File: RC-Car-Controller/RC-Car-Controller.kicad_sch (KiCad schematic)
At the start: 4 parts

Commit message: Fixed Controller PCB
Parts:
- D1, D2: footprint (none) -> LED_SMD:LED_0201_0603Metric
- R13: value R -> 1.5kohm; footprint (none) -> Resistor_SMD:R_0201_0603Metric
- R14: footprint (none) -> Resistor_SMD:R_0201_0603Metric
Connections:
- no-connect marks 3 -> 4
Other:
- removed sheet CurrentSense
- added sheet MiscDriver (MiscDriver.kicad_sch)
- sheet Connectors ports: added LIGHTS_PWM, NRST, RELAY_CTRL, RF_ANT, SWCLK, SWDIO, USART_RX, USART_TX; removed none
- sheet MCU ports: added LIGHTS_PWM, NRST, RELAY_CTRL, RF_NRST, SPI1_CS_RF, SPI1_MISO_RF, SPI1_MOSI_RF, SPI1_SCLK_RF, SWCLK, SWDIO, USART1_RX, USART1_TX; removed none
- sheet RF ports: added CS, IRQ, MISO, MOSI, RF_ANT, RSTN, SCLK; removed none
- note added: "Power"
- note removed: "Main"
- note removed: "Power Domains"

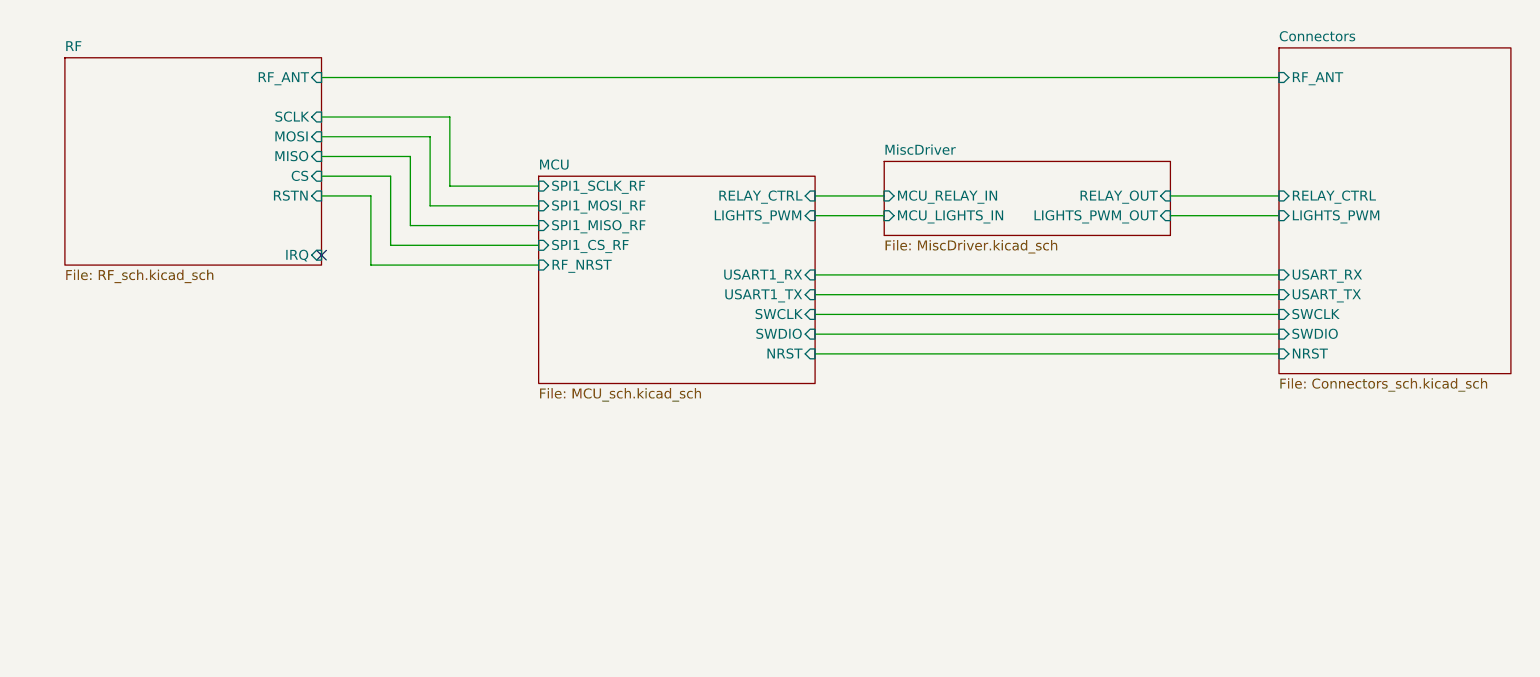
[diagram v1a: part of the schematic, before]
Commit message: Added IO to Controller
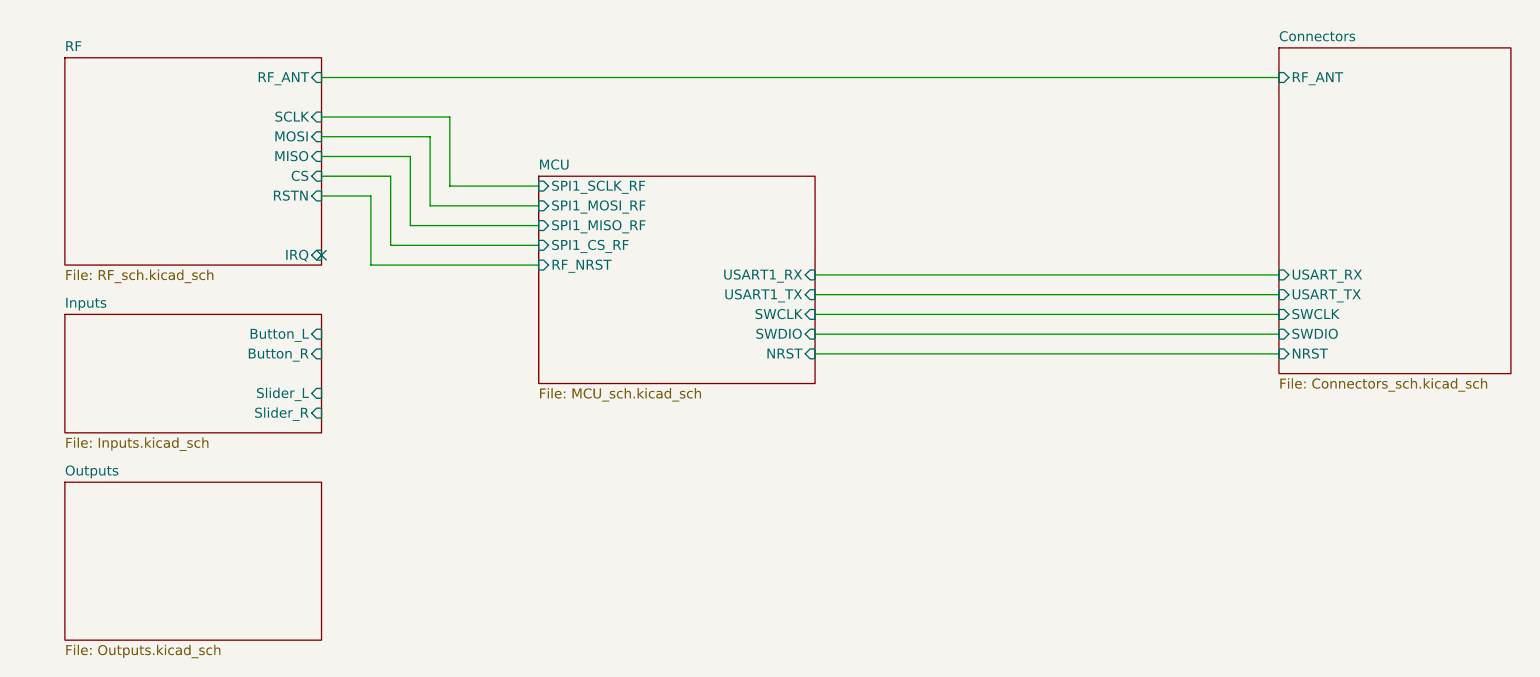
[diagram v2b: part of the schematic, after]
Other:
- removed sheet MiscDriver
- added sheet Inputs (Inputs.kicad_sch)
- added sheet Outputs (Outputs.kicad_sch)
- sheet Connectors ports: added none; removed LIGHTS_PWM, RELAY_CTRL
- sheet MCU ports: added none; removed LIGHTS_PWM, RELAY_CTRL
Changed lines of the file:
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@@
-	(wire
-		(pts
-			(xy 194.31 87.63) (xy 208.28 87.63)
-		)
-		(stroke
-			(width 0)
-			(type default)
-		)
-	)
 	(wire
 		(pts
@@
 	(wire
 		(pts
-			(xy 148.59 87.63) (xy 157.48 87.63)
-		)
-		(stroke
-			(width 0)
-			(type default)
-		)
-	)
-	(wire
-		(pts
 			(xy 85.09 80.01) (xy 96.52 80.01)
 		)
@@
 	(wire
 		(pts
-			(xy 148.59 85.09) (xy 157.48 85.09)
-		)
-		(stroke
-			(width 0)
-			(type default)
-		)
-	)
-	(wire
-		(pts
 			(xy 113.03 86.36) (xy 99.06 86.36)
-		)
-		(stroke
-			(width 0)
-			(type default)
-		)
-	)
-	(wire
-		(pts
-			(xy 194.31 85.09) (xy 208.28 85.09)
 		)
 		(stroke
@@
 	)
 	(sheet
+		(at 52.07 100.33)
+		(size 33.02 15.24)
+		(fields_autoplaced yes)
+		(stroke
+			(width 0.1524)
+			(type solid)
+		)
+		(fill
+			(color 0 0 0 0.0000)
+		)
+		(property "Sheetname" "Inputs"
+			(at 52.07 99.6184 0)
+			(effects
+				(font
+					(size 1.27 1.27)
+				)
+				(justify left bottom)
+			)
+		)
+		(property "Sheetfile" "Inputs.kicad_sch"
+			(at 52.07 116.1546 0)
+			(effects
+				(font
+					(size 1.27 1.27)
+				)
+				(justify left top)
+			)
+		)
+		(pin "Button_L" input
+			(at 85.09 102.87 0)
+			(effects
+				(font
+					(size 1.27 1.27)
+				)
+				(justify right)
+			)
+		)
+		(pin "Slider_R" input
+			(at 85.09 113.03 0)
+			(effects
+				(font
+					(size 1.27 1.27)
+				)
+				(justify right)
+			)
+		)
+		(pin "Slider_L" input
+			(at 85.09 110.49 0)
+			(effects
+				(font
+					(size 1.27 1.27)
+				)
+				(justify right)
+			)
+		)
+		(pin "Button_R" input
+			(at 85.09 105.41 0)
+			(effects
+				(font
+					(size 1.27 1.27)
+				)
+				(justify right)
+			)
+		)
+		(instances
+			(project "RC-Car-Controller"
+				(path "/ba870fd1-751d-4755-8e1a-1ea86ca9e2f6"
+					(page "7")
+				)
+			)
+		)
+	)
+	(sheet
 		(at 208.28 66.04)
 		(size 29.845 41.91)
@@
 				)
 				(justify left top)
-			)
-		)
-		(pin "RELAY_CTRL" input
-			(at 208.28 85.09 180)
-			(effects
-				(font
-					(size 1.27 1.27)
-				)
-				(justify left)
-			)
-		)
-		(pin "LIGHTS_PWM" input
-			(at 208.28 87.63 180)
-			(effects
-				(font
-					(size 1.27 1.27)
-				)
-				(justify left)
 			)
 		)
@@
 	)
 	(sheet
-		(at 157.48 80.645)
-		(size 36.83 9.525)
+		(at 113.03 82.55)
+		(size 35.56 26.67)
 		(fields_autoplaced yes)
 		(stroke
@@
 			(color 0 0 0 0.0000)
 		)
-		(property "Sheetname" "MiscDriver"
-			(at 157.48 79.9334 0)
+		(property "Sheetname" "MCU"
+			(at 113.03 81.8384 0)
 			(effects
 				(font
@@
 			)
 		)
-		(property "Sheetfile" "MiscDriver.kicad_sch"
-			(at 157.48 90.7546 0)
+		(property "Sheetfile" "MCU_sch.kicad_sch"
+			(at 113.03 109.8046 0)
 			(effects
 				(font
@@
 			)
 		)
-		(pin "MCU_RELAY_IN" input
-			(at 157.48 85.09 180)
+		(pin "SPI1_MISO_RF" input
+			(at 113.03 88.9 180)
 			(effects
 				(font
@@
 			)
 		)
-		(pin "MCU_LIGHTS_IN" input
-			(at 157.48 87.63 180)
+		(pin "SPI1_MOSI_RF" input
+			(at 113.03 86.36 180)
 			(effects
 				(font
@@
 			)
 		)
-		(pin "LIGHTS_PWM_OUT" input
-			(at 194.31 87.63 0)
-			(effects
-				(font
-					(size 1.27 1.27)
-				)
-				(justify right)
-			)
-		)
-		(pin "RELAY_OUT" input
-			(at 194.31 85.09 0)
-			(effects
-				(font
-					(size 1.27 1.27)
-				)
-				(justify right)
+		(pin "SPI1_SCLK_RF" input
+			(at 113.03 83.82 180)
+			(effects
+				(font
+					(size 1.27 1.27)
+				)
+				(justify left)
+			)
+		)
+		(pin "USART1_TX" input
+			(at 148.59 97.79 0)
+			(effects
+				(font
+					(size 1.27 1.27)
+				)
+				(justify right)
+			)
+		)
+		(pin "USART1_RX" input
+			(at 148.59 95.25 0)
+			(effects
+				(font
+					(size 1.27 1.27)
+				)
+				(justify right)
+			)
+		)
+		(pin "SPI1_CS_RF" input
+			(at 113.03 91.44 180)
+			(effects
+				(font
+					(size 1.27 1.27)
+				)
+				(justify left)
+			)
+		)
+		(pin "NRST" input
+			(at 148.59 105.41 0)
+			(effects
+				(font
+					(size 1.27 1.27)
+				)
+				(justify right)
+			)
+		)
+		(pin "SWDIO" input
+			(at 148.59 102.87 0)
+			(effects
+				(font
+					(size 1.27 1.27)
+				)
+				(justify right)
+			)
+		)
+		(pin "SWCLK" input
+			(at 148.59 100.33 0)
+			(effects
+				(font
+					(size 1.27 1.27)
+				)
+				(justify right)
+			)
+		)
+		(pin "RF_NRST" input
+			(at 113.03 93.98 180)
+			(effects
+				(font
+					(size 1.27 1.27)
+				)
+				(justify left)
 			)
 		)
@@
 			(project "RC-Car-Controller"
 				(path "/ba870fd1-751d-4755-8e1a-1ea86ca9e2f6"
-					(page "8")
+					(page "4")
 				)
 			)
@@
 	)
 	(sheet
-		(at 113.03 82.55)
-		(size 35.56 26.67)
+		(at 52.07 121.92)
+		(size 33.02 20.32)
 		(fields_autoplaced yes)
 		(stroke
@@
 			(color 0 0 0 0.0000)
 		)
-		(property "Sheetname" "MCU"
-			(at 113.03 81.8384 0)
+		(property "Sheetname" "Outputs"
+			(at 52.07 121.2084 0)
 			(effects
 				(font
@@
 			)
 		)
-		(property "Sheetfile" "MCU_sch.kicad_sch"
-			(at 113.03 109.8046 0)
+		(property "Sheetfile" "Outputs.kicad_sch"
+			(at 52.07 142.8246 0)
 			(effects
 				(font
@@
 			)
 		)
-		(pin "SPI1_MISO_RF" input
-			(at 113.03 88.9 180)
-			(effects
-				(font
-					(size 1.27 1.27)
-				)
-				(justify left)
-			)
-		)
-		(pin "SPI1_MOSI_RF" input
-			(at 113.03 86.36 180)
-			(effects
-				(font
-					(size 1.27 1.27)
-				)
-				(justify left)
-			)
-		)
-		(pin "SPI1_SCLK_RF" input
-			(at 113.03 83.82 180)
-			(effects
-				(font
-					(size 1.27 1.27)
-				)
-				(justify left)
-			)
-		)
-		(pin "USART1_TX" input
-			(at 148.59 97.79 0)
-			(effects
-				(font
-					(size 1.27 1.27)
-				)
-				(justify right)
-			)
-		)
-		(pin "USART1_RX" input
-			(at 148.59 95.25 0)
-			(effects
-				(font
-					(size 1.27 1.27)
-				)
-				(justify right)
-			)
-		)
-		(pin "RELAY_CTRL" input
-			(at 148.59 85.09 0)
-			(effects
-				(font
-					(size 1.27 1.27)
-				)
-				(justify right)
-			)
-		)
-		(pin "SPI1_CS_RF" input
-			(at 113.03 91.44 180)
-			(effects
-				(font
-					(size 1.27 1.27)
-				)
-				(justify left)
-			)
-		)
-		(pin "NRST" input
-			(at 148.59 105.41 0)
-			(effects
-				(font
-					(size 1.27 1.27)
-				)
-				(justify right)
-			)
-		)
-		(pin "SWDIO" input
-			(at 148.59 102.87 0)
-			(effects
-				(font
-					(size 1.27 1.27)
-				)
-				(justify right)
-			)
-		)
-		(pin "SWCLK" input
-			(at 148.59 100.33 0)
-			(effects
-				(font
-					(size 1.27 1.27)
-				)
-				(justify right)
-			)
-		)
-		(pin "RF_NRST" input
-			(at 113.03 93.98 180)
-			(effects
-				(font
-					(size 1.27 1.27)
-				)
-				(justify left)
-			)
-		)
-		(pin "LIGHTS_PWM" input
-			(at 148.59 87.63 0)
-			(effects
-				(font
-					(size 1.27 1.27)
-				)
-				(justify right)
-			)
-		)
 		(instances
 			(project "RC-Car-Controller"
 				(path "/ba870fd1-751d-4755-8e1a-1ea86ca9e2f6"
-					(page "4")
-				)
-			)
+					(page "8")
+				)
+			)

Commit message: Finished prelim. Controller
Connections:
- no-connect marks 4 -> 6
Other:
- added sheet ADC (adc.kicad_sch)
- sheet MCU ports: added ALERT_GPIO, BTN_L, BTN_R, I2C1_SCL, I2C1_SDA, I2C2_SCL, I2C2_SDA, SPI2_CS_LCD, SPI2_MISO, SPI2_MOSI, SPI2_SCLK, SPI3_CS_ADC, SPI3_MISO, SPI3_MOSI, SPI3_SCLK, SPI4_CS_RF, SPI4_MISO_RF, SPI4_MOSI_RF, SPI4_SCLK_RF, WIPE_L, WIPE_R; removed SPI1_CS_RF, SPI1_MISO_RF, SPI1_MOSI_RF, SPI1_SCLK_RF
- sheet Outputs ports: added LCD_CLK, LCD_CS, LCD_DC, LCD_DIN, LCD_RST, OLED_L_SCL, OLED_L_SDA, OLED_R_SCL, OLED_R_SDA; removed none

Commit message: Did some stuff on the Controller
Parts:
- removed R13: 1.5kohm, Resistor_SMD:R_0201_0603Metric, symbol Device:R
- removed R14: 220ohm, Resistor_SMD:R_0201_0603Metric, symbol Device:R
- added R7: 1.5kohm, Resistor_SMD:R_0603_1608Metric, symbol Device:R
- added R8: 220ohm, Resistor_SMD:R_0603_1608Metric, symbol Device:R
- D1, D2: footprint LED_SMD:LED_0201_0603Metric -> LED_SMD:LED_0603_1608Metric
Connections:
- net +3V3: now also R8.1
- net VDD_BATT: now also R7.1
- net at D1.2 (A): now also R7.2
- net at D2.2 (A): now also R8.2
- no-connect marks 6 -> 8
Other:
- sheet Connectors ports: added CON_USB_D+, CON_USB_D-; removed none
- sheet MCU ports: added MCU_USB_D+, MCU_USB_D-; removed none
- note added: "SWITCH"

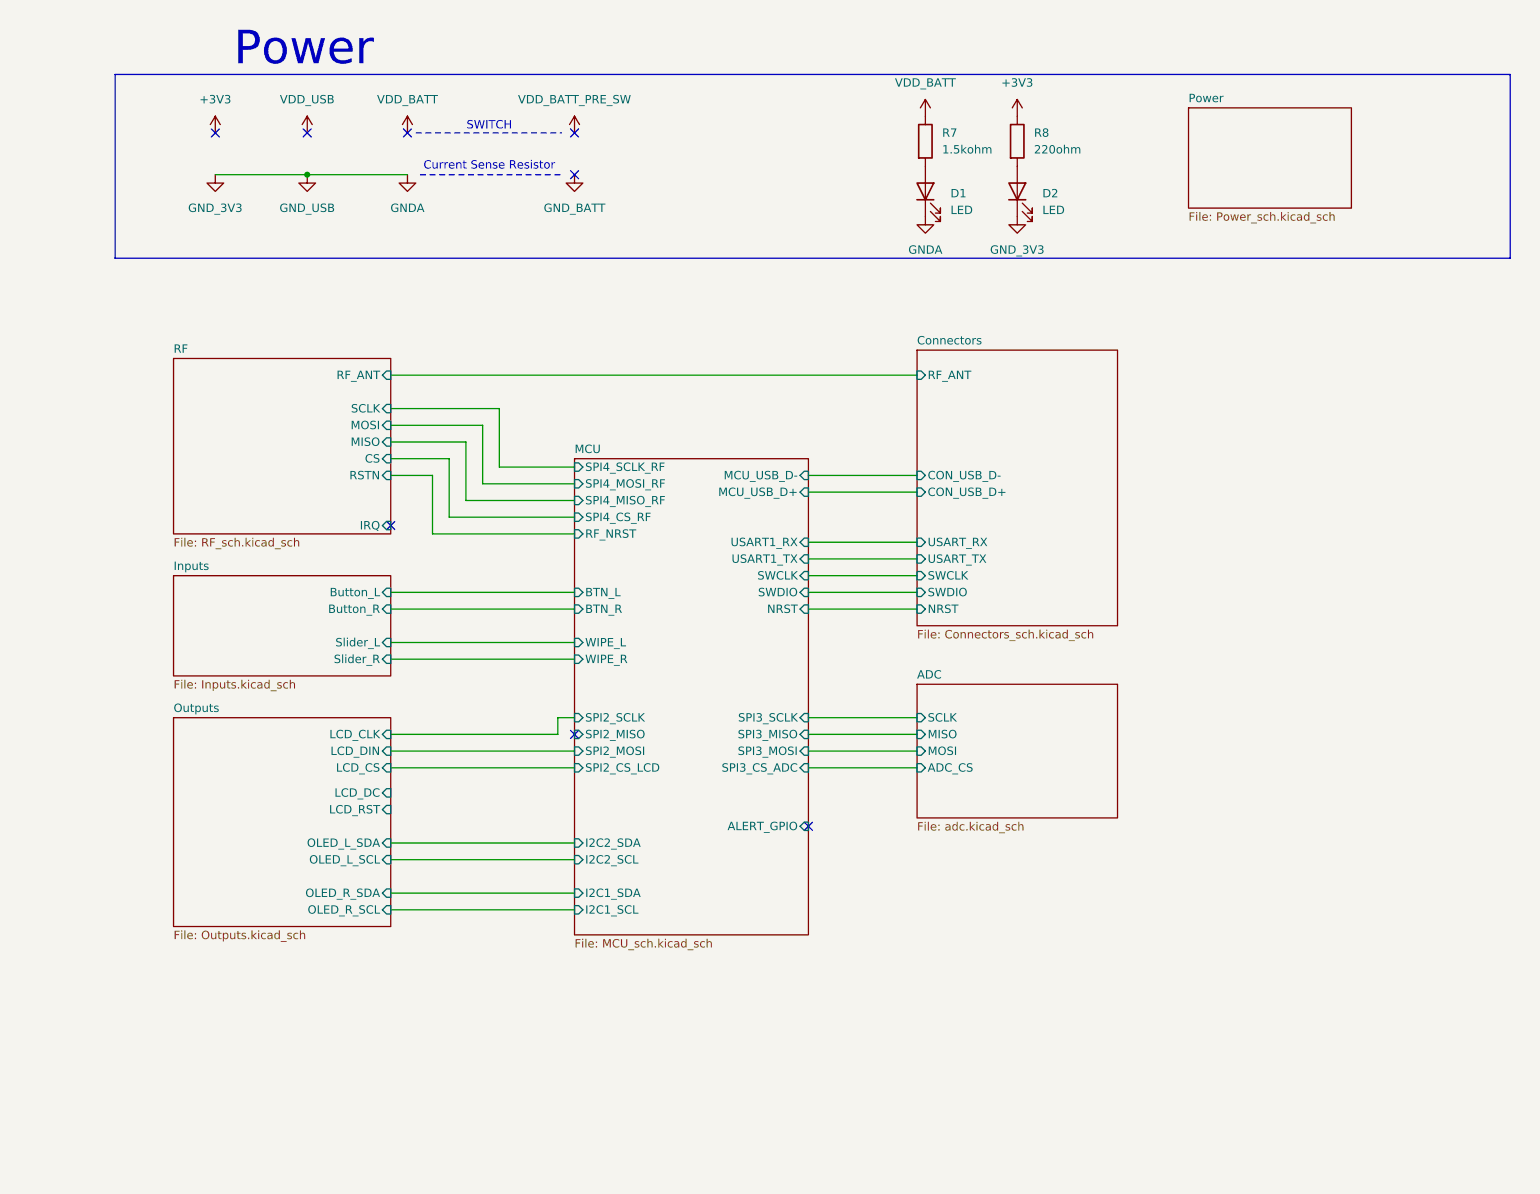
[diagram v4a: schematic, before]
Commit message: Fixed LiPo Charge/Monitor Circuitry
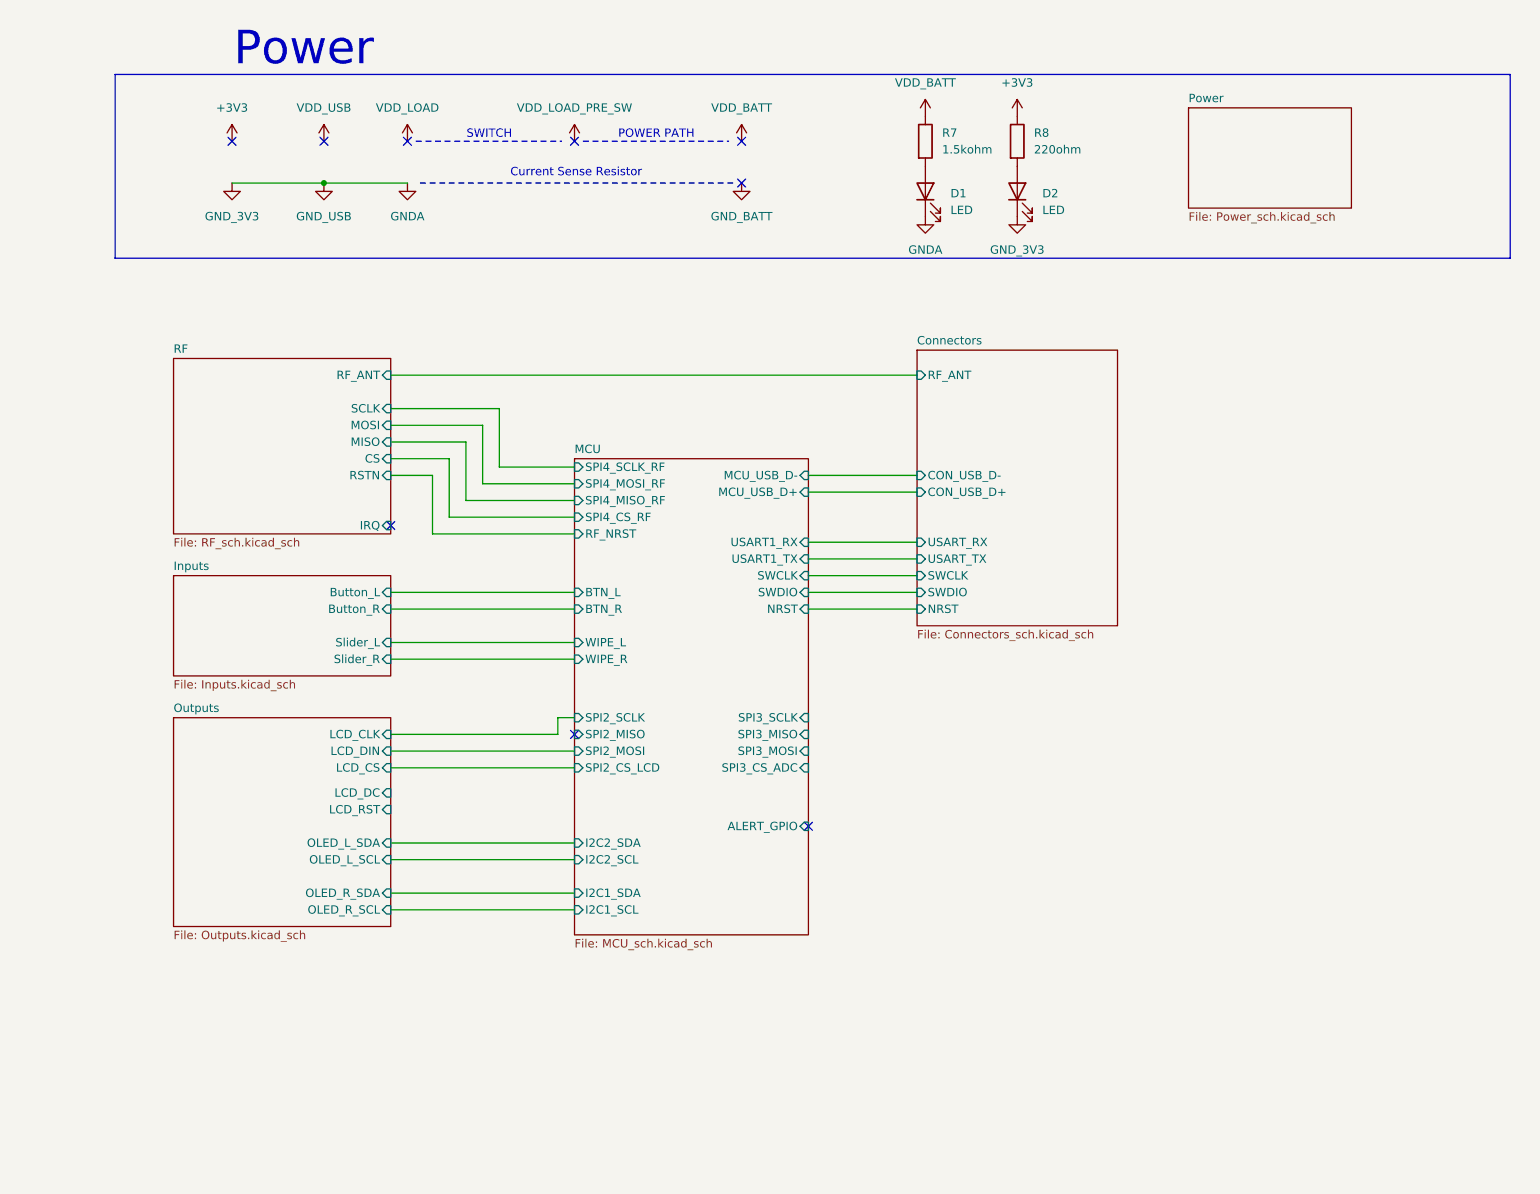
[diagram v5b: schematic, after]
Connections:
- no-connect marks 8 -> 9
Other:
- removed sheet ADC
- note added: "POWER PATH"
